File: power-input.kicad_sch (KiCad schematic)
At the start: 27 parts, among them J1 PJ-018, J2 MDT420E03002, Q1 TSM9409CS, Q2 TSM9409CS, Q3 TSM9409CS, U1 TPS54331DRG4

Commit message: Add BMS
Signed-off-by: JeffMboya <jangina.mboya@gmail.com>
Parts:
- removed J2: MDT420E03002, MDT420E03002:AMPHENOL_MDT420E03002, symbol MDT420E03002:MDT420E03002
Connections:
- no-connect marks 56 -> 0
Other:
- company: (none) -> ABTTRACT MACHINES
- title: (none) -> M.2 E-KEY SOCKET
- moved on the sheet: C1, C2, C3, C4, R4, R5, R7, U1

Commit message: Add BMS
Signed-off-by: JeffMboya <jangina.mboya@gmail.com>
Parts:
- added C11, C12: 22uF, Capacitor_SMD:C_1206_3216Metric, symbol Device:C
- added R17, R18: 100, Resistor_SMD:R_0603_1608Metric, symbol Device:R
- added U4: MT3608, MT3608:SOT95P280X145-6N, symbol MT3608:MT3608
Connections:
- net +3V3: now also C11.1, C12.1, R17.1, U4.1 (SW), U4.4 (EN), U4.5 (IN)
- net GND: now also C11.2, C12.2, R18.2, U4.2 (GND)
- new net: R17.2, R18.1, U4.3 (FB)
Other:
- note added: "3v3 DC to 5v DC boost converter"

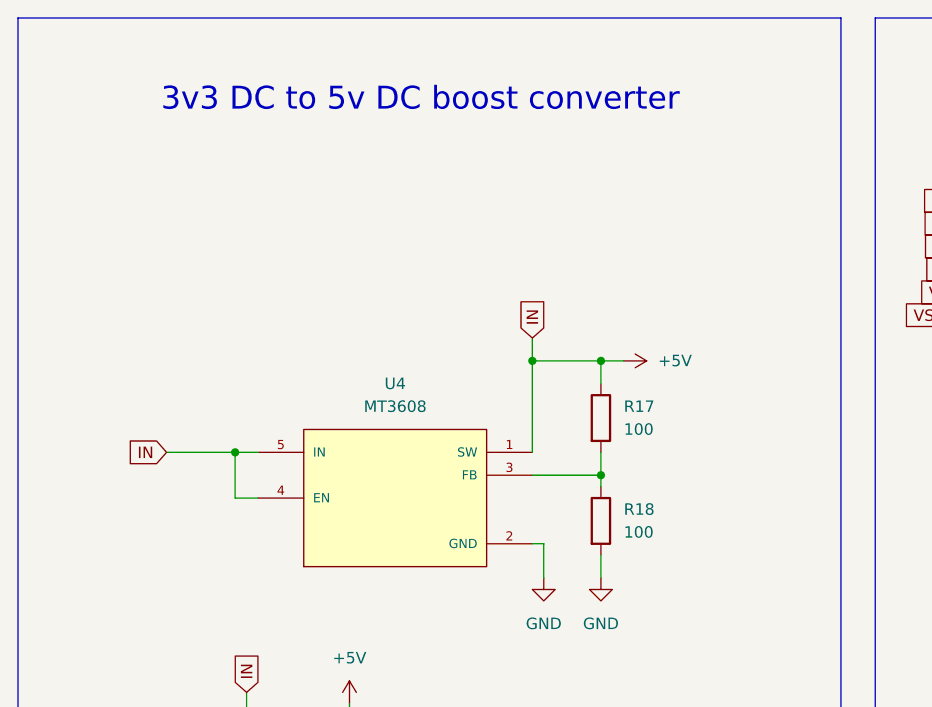
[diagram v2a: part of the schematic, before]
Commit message: Add boost converter
Signed-off-by: JeffMboya <jangina.mboya@gmail.com>
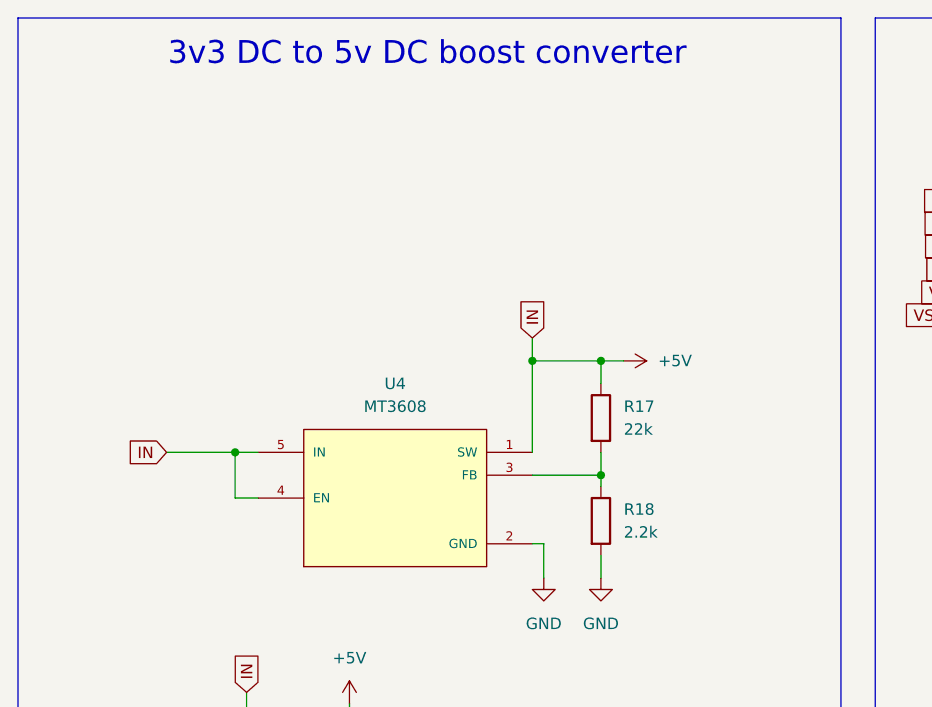
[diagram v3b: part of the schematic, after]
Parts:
- R17: value 100 -> 22k
- R18: value 100 -> 2.2k
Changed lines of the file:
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@@
 	(text "3v3 DC to 5v DC boost converter"
 		(exclude_from_sim no)
-		(at 63.754 24.384 0)
+		(at 64.516 19.304 0)
 		(effects
 			(font
@@
 			)
 		)
-		(property "Value" "100"
+		(property "Value" "2.2k"
 			(at 86.36 72.3899 0)
 			(effects
@@
 			)
 		)
-		(property "Value" "100"
+		(property "Value" "22k"
 			(at 86.36 60.9599 0)
 			(effects

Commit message: Update PCB
Signed-off-by: JeffMboya <jangina.mboya@gmail.com>
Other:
- moved on the sheet: R17, R18, U4

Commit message: Update PCB
Signed-off-by: JeffMboya <jangina.mboya@gmail.com>
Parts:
- removed R6: 0ZCA0100FF2E, 0ZCA0100FF2E:RESC3216X125N, symbol 0ZCA0100FF2E:0ZCA0100FF2E
- added F1: Fuse, Fuse:Fuse_0402_1005Metric, symbol Device:Fuse
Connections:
- net +9V: now also F1.2
- net at Q3.5, Q3.6, Q3.7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: now also F1.1
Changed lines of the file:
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@@
 	(wire
 		(pts
+			(xy 129.54 144.78) (xy 144.78 144.78)
+		)
+		(stroke
+			(width 0)
+			(type default)
+		)
+	)
+	(wire
+		(pts
 			(xy 231.14 106.68) (xy 242.57 106.68)
 		)
@@
 	(wire
 		(pts
-			(xy 137.16 144.78) (xy 144.78 144.78)
-		)
-		(stroke
-			(width 0)
-			(type default)
-		)
-	)
-	(wire
-		(pts
 			(xy 165.1 55.88) (xy 162.56 55.88)
 		)
@@
 	)
 	(symbol
-		(lib_id "0ZCA0100FF2E:0ZCA0100FF2E")
-		(at 129.54 144.78 0)
-		(unit 1)
-		(exclude_from_sim no)
-		(in_bom yes)
-		(on_board yes)
-		(dnp no)
-		(fields_autoplaced yes)
-		(property "Reference" "R6"
-			(at 129.54 138.43 0)
-			(effects
-				(font
-					(size 1.27 1.27)
-				)
-			)
-		)
-		(property "Value" "0ZCA0100FF2E"
-			(at 129.54 140.97 0)
-			(effects
-				(font
-					(size 1.27 1.27)
-				)
-				(hide yes)
-			)
-		)
-		(property "Footprint" "0ZCA0100FF2E:RESC3216X125N"
-			(at 129.54 144.78 0)
-			(effects
-				(font
-					(size 1.27 1.27)
-				)
-				(justify bottom)
-				(hide yes)
-			)
-		)
-		(property "Datasheet" ""
-			(at 129.54 144.78 0)
-			(effects
-				(font
-					(size 1.27 1.27)
-				)
-				(hide yes)
-			)
-		)
-		(property "Description" ""
-			(at 129.54 144.78 0)
-			(effects
-				(font
-					(size 1.27 1.27)
-				)
-				(hide yes)
-			)
-		)
-		(property "MF" "Bel Fuse"
-			(at 129.54 144.78 0)
-			(effects
-				(font
-					(size 1.27 1.27)
-				)
-				(justify bottom)
-				(hide yes)
-			)
-		)
-		(property "Description_1" "\n                        \n                            Polymeric PTC Resettable Fuse 6V 1 A Ih Surface Mount 1206 (3216 Metric), Concave\n                        \n"
-			(at 129.54 144.78 0)
-			(effects
-				(font
-					(size 1.27 1.27)
-				)
-				(justify bottom)
-				(hide yes)
-			)
-		)
-		(property "Package" "1206 Bel Fuse"
-			(at 129.54 144.78 0)
-			(effects
-				(font
-					(size 1.27 1.27)
-				)
-				(justify bottom)
-				(hide yes)
-			)
-		)
-		(property "Price" "None"
-			(at 129.54 144.78 0)
-			(effects
-				(font
-					(size 1.27 1.27)
-				)
-				(justify bottom)
-				(hide yes)
-			)
-		)
-		(property "SnapEDA_Link" "https://www.snapeda.com/parts/0ZCA0100FF2E/Bel+Fuse+Inc./view-part/?ref=snap"
-			(at 129.54 144.78 0)
-			(effects
-				(font
-					(size 1.27 1.27)
-				)
-				(justify bottom)
-				(hide yes)
-			)
-		)
-		(property "MP" "0ZCA0100FF2E"
-			(at 129.54 144.78 0)
-			(effects
-				(font
-					(size 1.27 1.27)
-				)
-				(justify bottom)
-				(hide yes)
-			)
-		)
-		(property "Availability" "In Stock"
-			(at 129.54 144.78 0)
-			(effects
-				(font
-					(size 1.27 1.27)
-				)
-				(justify bottom)
-				(hide yes)
-			)
-		)
-		(property "Check_prices" "https://www.snapeda.com/parts/0ZCA0100FF2E/Bel+Fuse+Inc./view-part/?ref=eda"
-			(at 129.54 144.78 0)
-			(effects
-				(font
-					(size 1.27 1.27)
-				)
-				(justify bottom)
-				(hide yes)
-			)
-		)
-		(pin "1"
-		)
-		(pin "2"
-		)
-		(instances
-			(project "e-key-slot"
-				(path "/c124244a-3c1c-475d-932f-950445d8391e/db23d5e1-a70c-4fb7-9aaa-94502e21acbf"
-					(reference "R6")
-					(unit 1)
-				)
-			)
-		)
-	)
-	(symbol
 		(lib_id "Device:R")
 		(at 52.07 162.56 0)
@@
 					(unit 1)
 				)
+			)
+		)
+	)
+	(symbol
+		(lib_id "Device:Fuse")
+		(at 125.73 144.78 90)
+		(unit 1)
+		(exclude_from_sim no)
+		(in_bom yes)
+		(on_board yes)
+		(dnp no)
+		(fields_autoplaced yes)
+		(property "Reference" "F1"
+			(at 125.73 138.43 90)
+			(effects
+				(font
+					(size 1.27 1.27)
+				)
+			)
+		)
+		(property "Value" "Fuse"
+			(at 125.73 140.97 90)
+			(effects
+				(font
+					(size 1.27 1.27)
+				)
+			)
+		)
+		(property "Footprint" "Fuse:Fuse_0402_1005Metric"
+			(at 125.73 146.558 90)
+			(effects
+				(font
+					(size 1.27 1.27)
+				)
+				(hide yes)
+			)
+		)
+		(property "Datasheet" "~"
+			(at 125.73 144.78 0)
+			(effects
+				(font
+					(size 1.27 1.27)
+				)
+				(hide yes)
+			)
+		)
+		(property "Description" "Fuse"
+			(at 125.73 144.78 0)
+			(effects
+				(font
+					(size 1.27 1.27)
+				)
+				(hide yes)
+			)
+		)
+		(pin "1"
+		)
+		(pin "2"
+		)
+		(instances
+			(project ""
+				(path "/c124244a-3c1c-475d-932f-950445d8391e/db23d5e1-a70c-4fb7-9aaa-94502e21acbf"
+					(reference "F1")
+					(unit 1)
+				)
